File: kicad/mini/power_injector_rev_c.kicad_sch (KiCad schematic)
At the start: 15 parts, among them J2 A00-108-220-450, J3 A00-108-220-450, J4 JACK-PLUG0

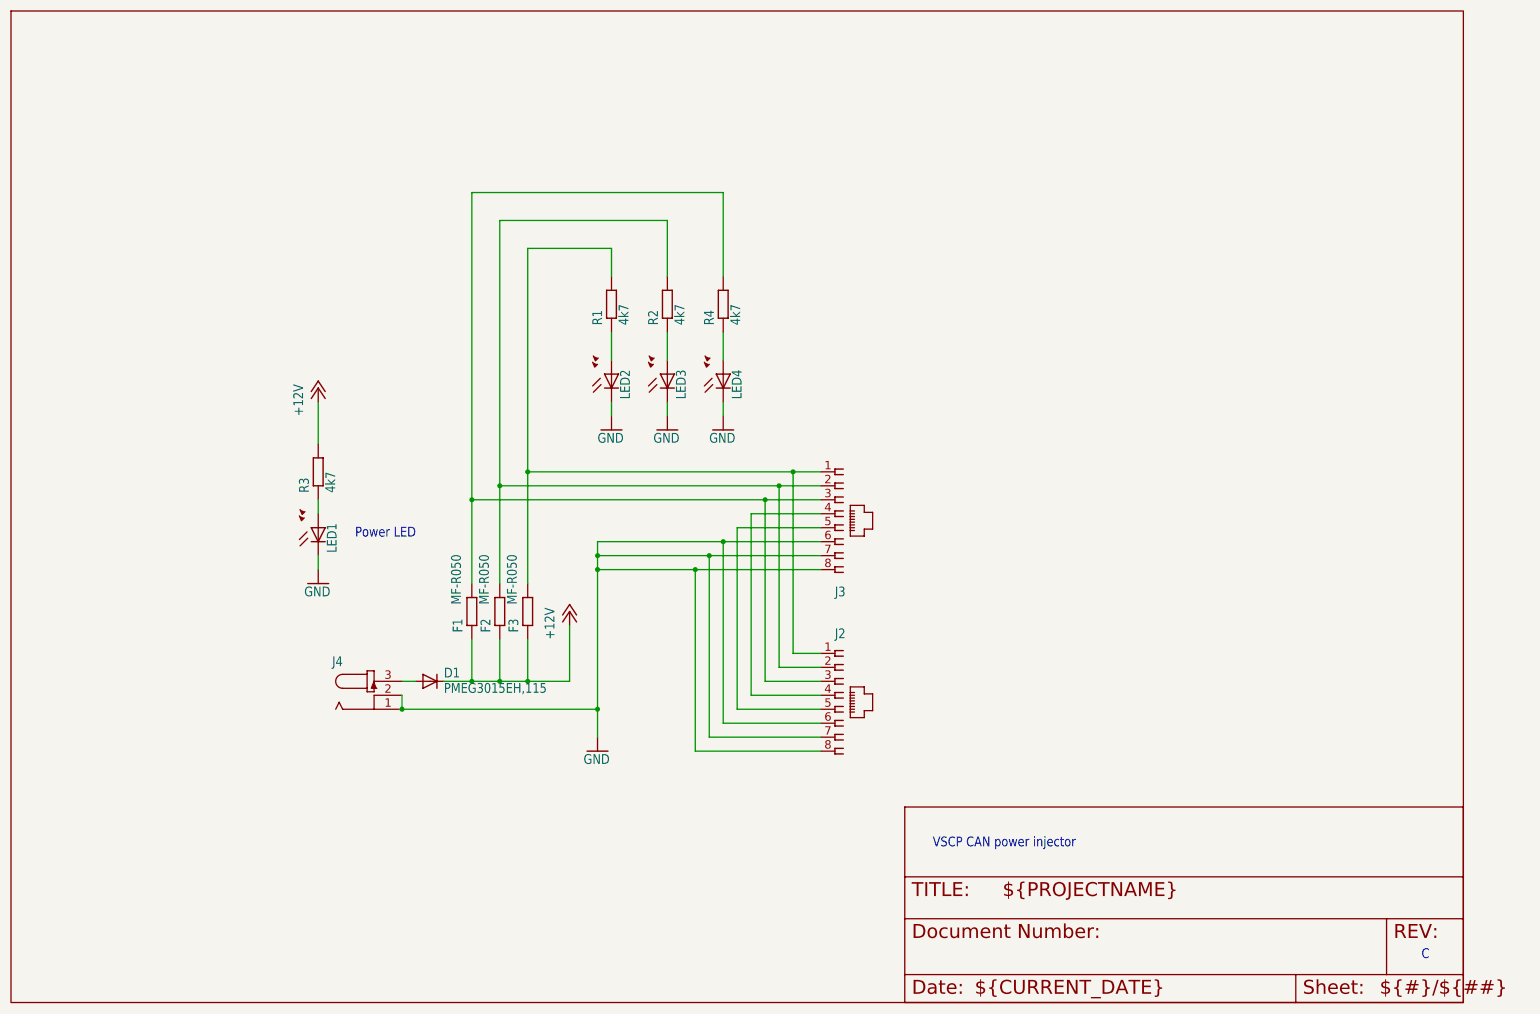
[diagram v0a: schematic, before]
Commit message: Rearranged files (in a more logical way)
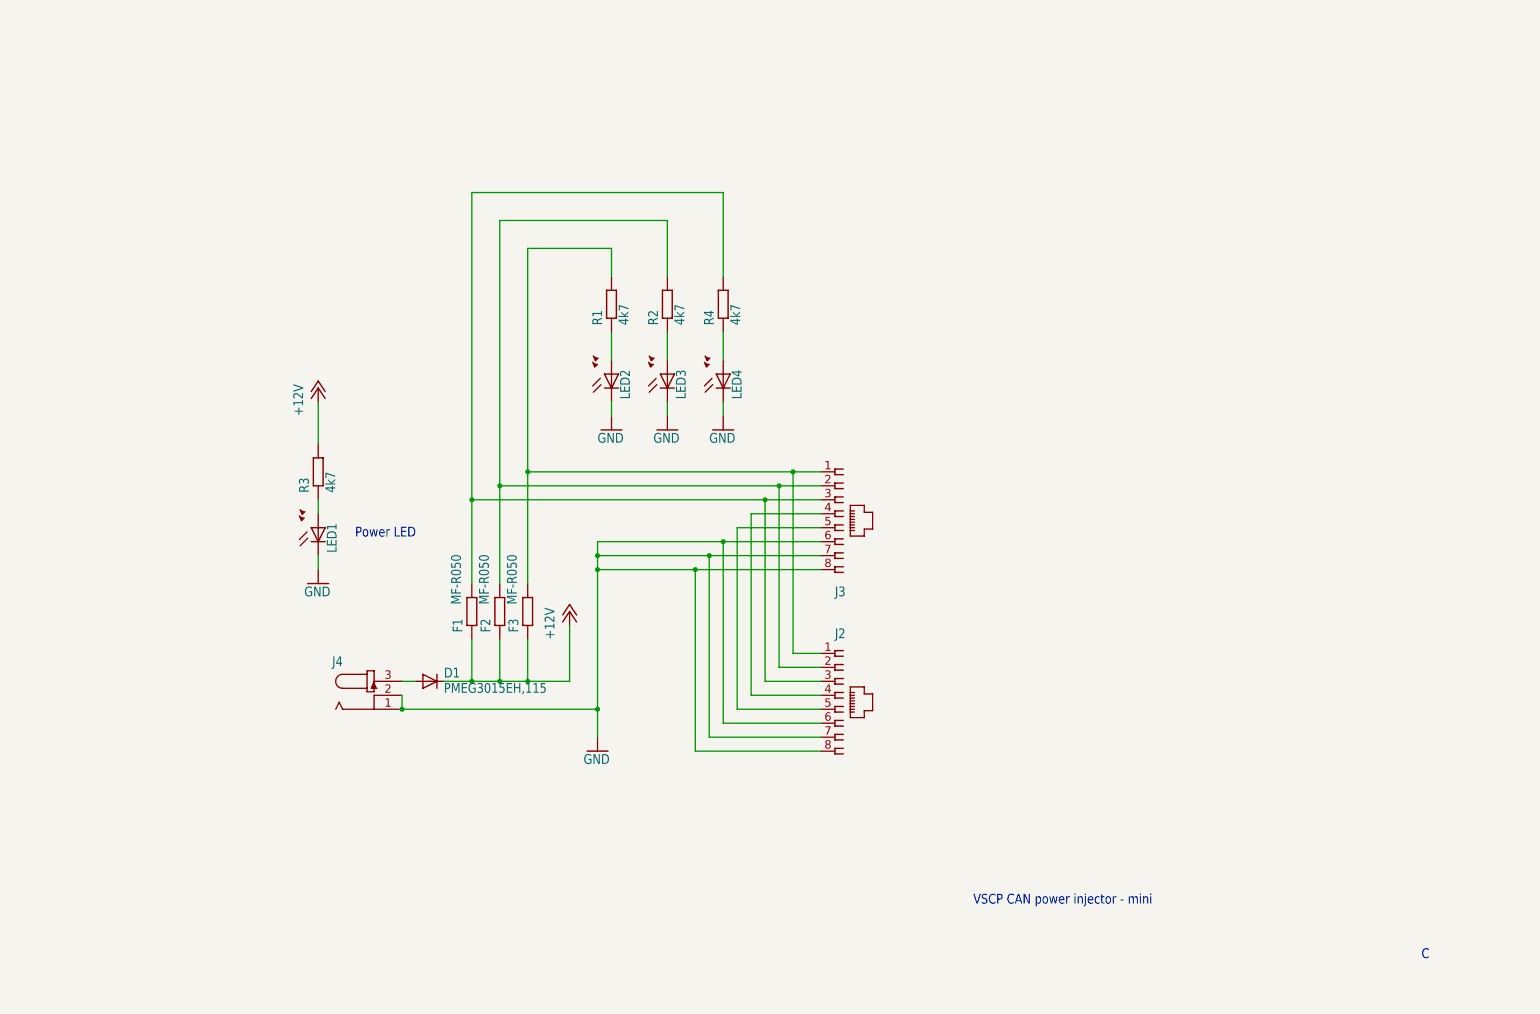
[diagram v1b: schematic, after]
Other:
- note added: "VSCP CAN power injector - mini"
- note removed: "VSCP CAN power injector"
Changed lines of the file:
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@@
 		)
 	)
-	(text "VSCP CAN power injector"
+	(text "VSCP CAN power injector - mini"
 		(exclude_from_sim no)
-		(at 185.42 170.18 0)
+		(at 192.786 180.594 0)
 		(effects
 			(font
@@
 			(width 0.1524)
 			(type solid)
-		)
-	)
-	(symbol
-		(lib_id "power_injector_rev_c-eagle-import:DINA4_L")
-		(at 180.34 198.12 0)
-		(unit 2)
-		(exclude_from_sim no)
-		(in_bom yes)
-		(on_board yes)
-		(dnp no)
-		(property "Reference" "#FRAME1"
-			(at 180.34 198.12 0)
-			(effects
-				(font
-					(size 1.27 1.27)
-				)
-				(hide yes)
-			)
-		)
-		(property "Value" "DINA4_L"
-			(at 180.34 198.12 0)
-			(effects
-				(font
-					(size 1.27 1.27)
-				)
-				(hide yes)
-			)
-		)
-		(property "Footprint" ""
-			(at 180.34 198.12 0)
-			(effects
-				(font
-					(size 1.27 1.27)
-				)
-				(hide yes)
-			)
-		)
-		(property "Datasheet" ""
-			(at 180.34 198.12 0)
-			(effects
-				(font
-					(size 1.27 1.27)
-				)
-				(hide yes)
-			)
-		)
-		(property "Description" ""
-			(at 180.34 198.12 0)
-			(effects
-				(font
-					(size 1.27 1.27)
-				)
-				(hide yes)
-			)
-		)
-		(instances
-			(project ""
-				(path "/7423aa41-8104-411d-b4c9-a3ca20e8cc07"
-					(reference "#FRAME1")
-					(unit 2)
-				)
-			)
 		)
 	)
@@
 					(unit 1)
 				)
-			)
-		)
-	)
-	(symbol
-		(lib_id "power_injector_rev_c-eagle-import:DINA4_L")
-		(at 17.78 198.12 0)
-		(unit 1)
-		(exclude_from_sim no)
-		(in_bom yes)
-		(on_board yes)
-		(dnp no)
-		(property "Reference" "#FRAME1"
-			(at 17.78 198.12 0)
-			(effects
-				(font
-					(size 1.27 1.27)
-				)
-				(hide yes)
-			)
-		)
-		(property "Value" "DINA4_L"
-			(at 17.78 198.12 0)
-			(effects
-				(font
-					(size 1.27 1.27)
-				)
-				(hide yes)
-			)
-		)
-		(property "Footprint" ""
-			(at 17.78 198.12 0)
-			(effects
-				(font
-					(size 1.27 1.27)
-				)
-				(hide yes)
-			)
-		)
-		(property "Datasheet" ""
-			(at 17.78 198.12 0)
-			(effects
-				(font
-					(size 1.27 1.27)
-				)
-				(hide yes)
-			)
-		)
-		(property "Description" ""
-			(at 17.78 198.12 0)
-			(effects
-				(font
-					(size 1.27 1.27)
-				)
-				(hide yes)
-			)
-		)
-		(instances
-			(project ""
-				(path "/7423aa41-8104-411d-b4c9-a3ca20e8cc07"
-					(reference "#FRAME1")
-					(unit 1)
-				)
